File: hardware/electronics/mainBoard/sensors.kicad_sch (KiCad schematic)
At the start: 8 parts, among them J18 M8S-04PFFR-SF8001, J19 STEMMA-QT, J20 STEMMA-QT, J21 STEMMA-QT, J22 STEMMA-QT, J23 STEMMA-QT, U18 LPS28DFW

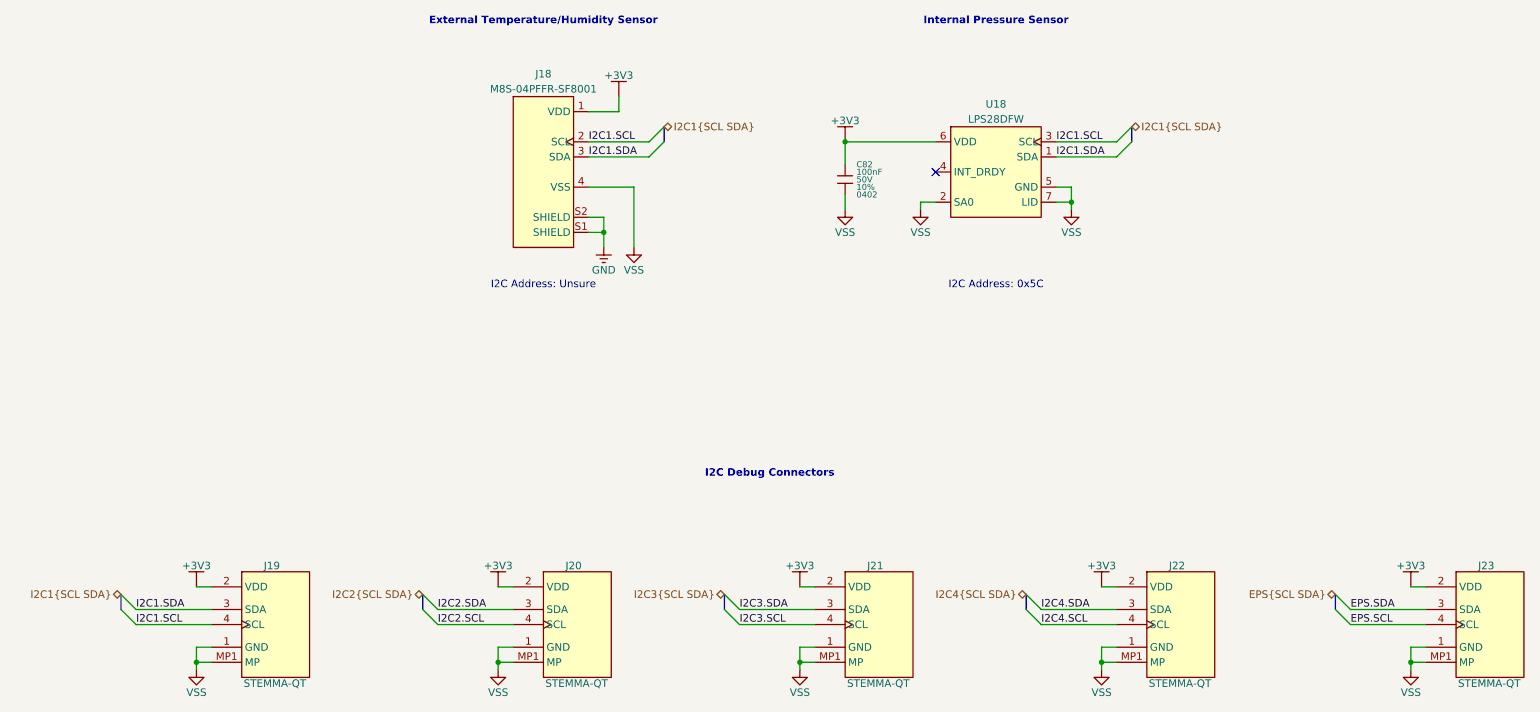
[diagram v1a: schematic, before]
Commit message: moved STEMA QT connectors to debugger sheets
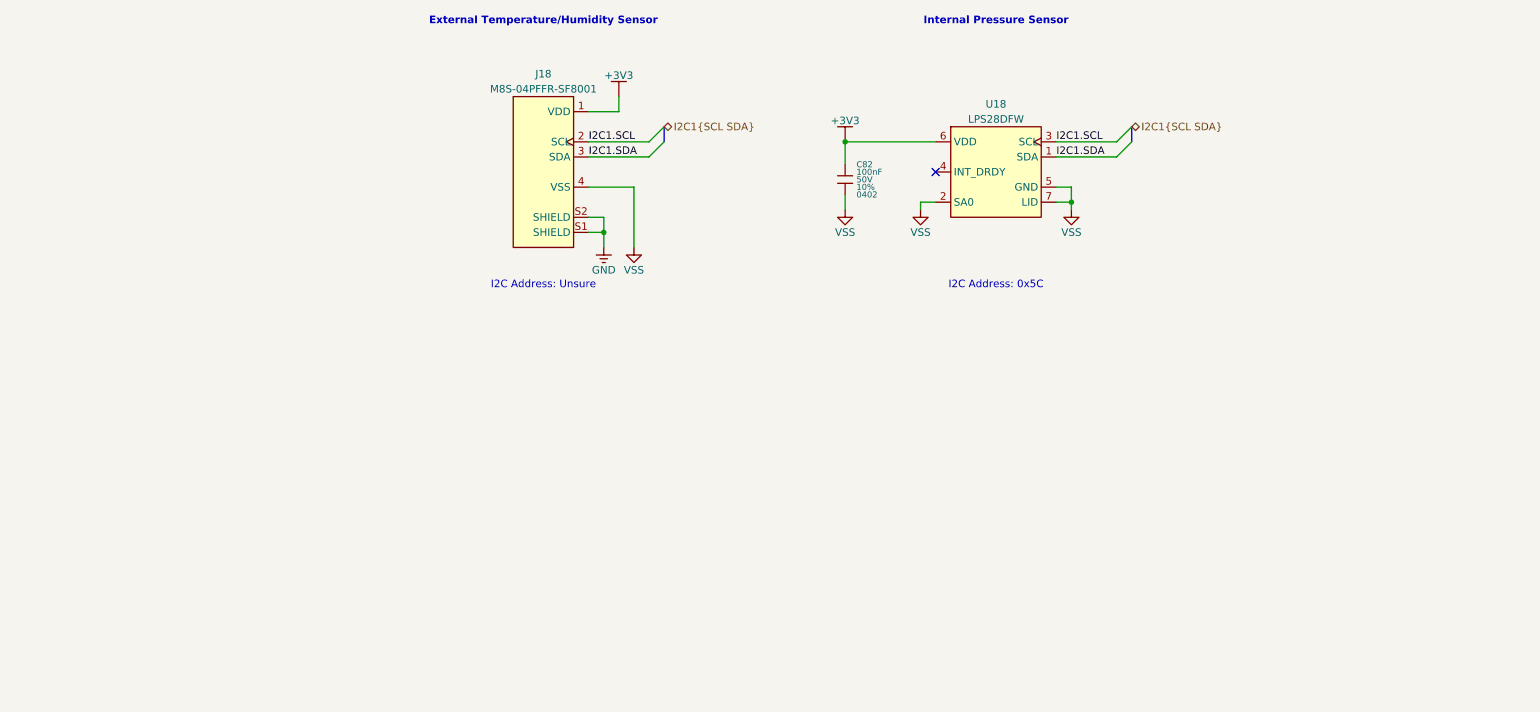
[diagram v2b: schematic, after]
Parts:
- removed J19, J20, J21, J22, J23: STEMMA-QT, lib_connectors:JST_SH_BM04B-SRSS-TB, symbol lib_sch:STEMMA-QT
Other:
- note removed: "I2C Debug Connectors"

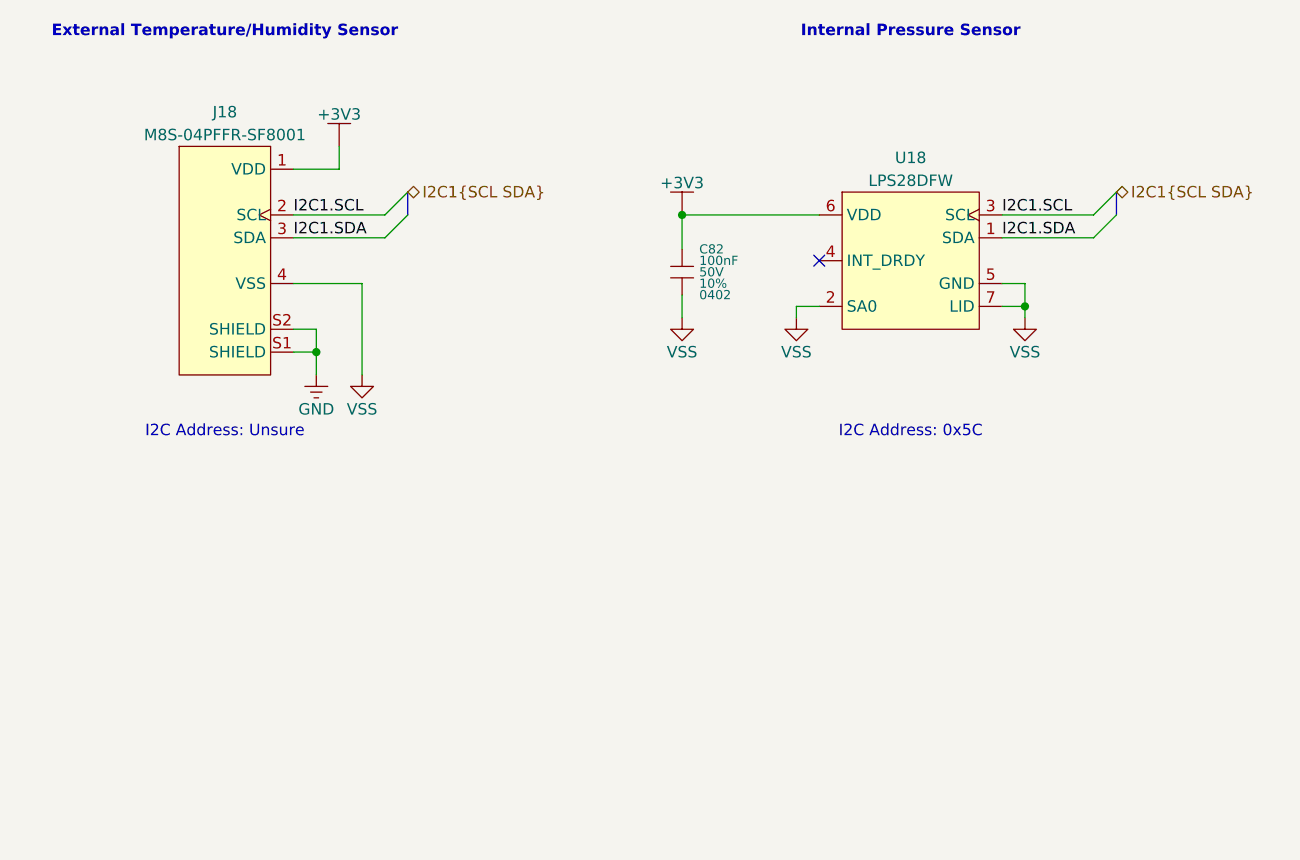
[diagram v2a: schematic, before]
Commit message: fixed net names and added notes
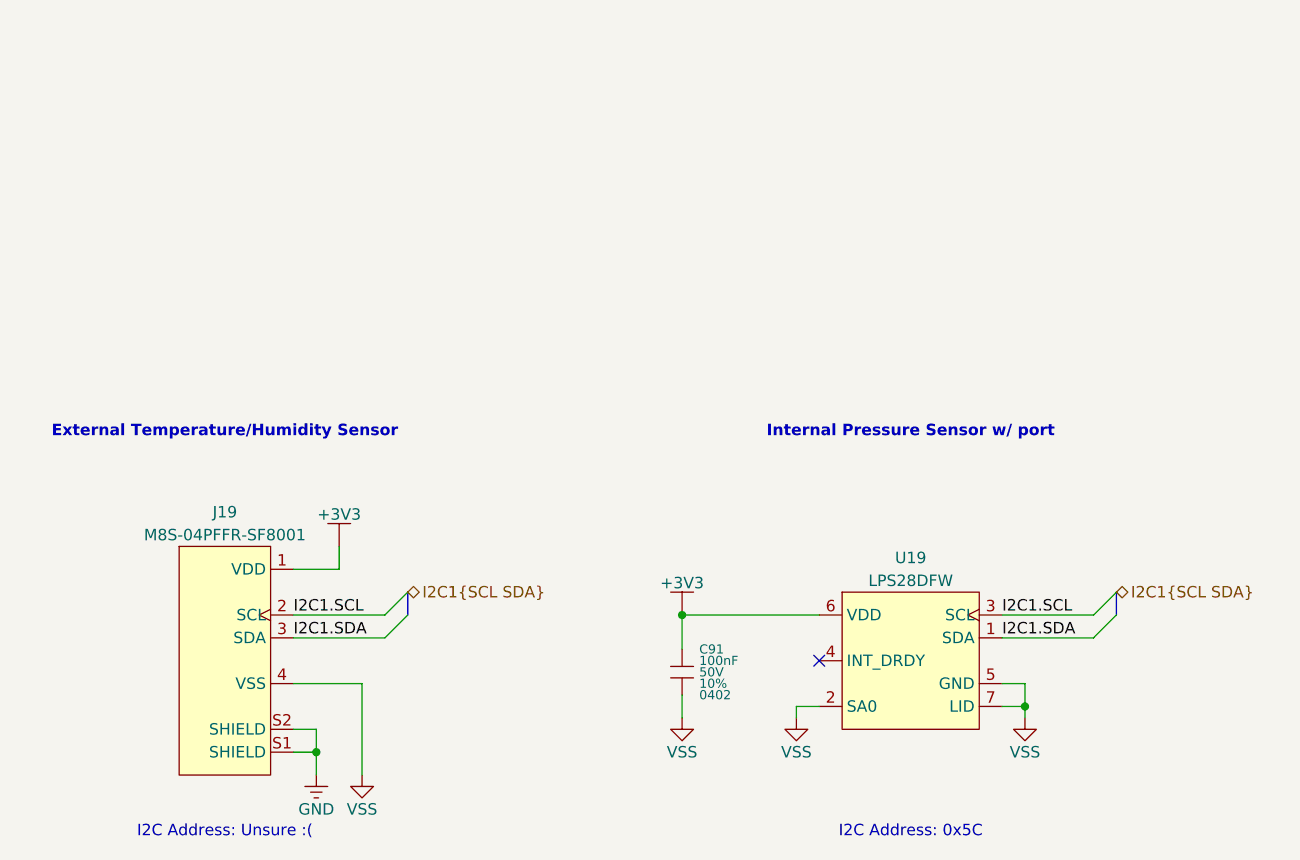
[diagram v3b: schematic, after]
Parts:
- renumbered C82 to C91, J18 to J19, U18 to U19
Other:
- note added: "I2C Address: Unsure :("
- note added: "Internal Pressure Sensor w/ port"
- note removed: "I2C Address: Unsure"
- note removed: "Internal Pressure Sensor"
- moved on the sheet: C91, J19, U19

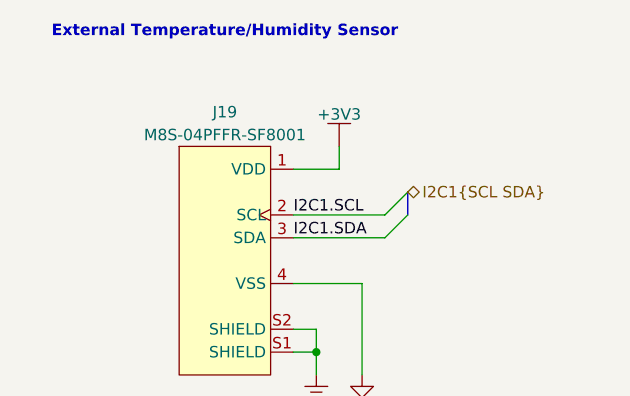
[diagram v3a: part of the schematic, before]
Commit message: renumber references
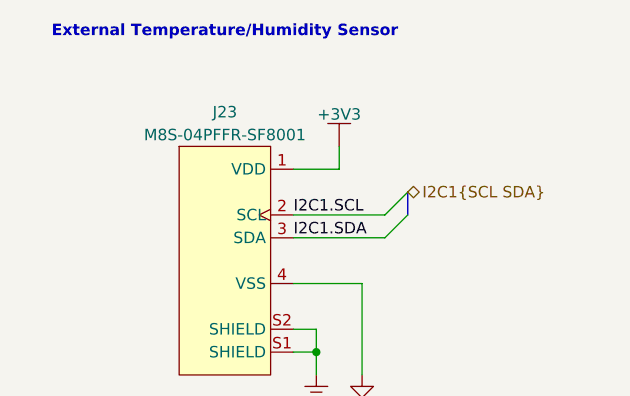
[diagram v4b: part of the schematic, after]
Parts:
- renumbered J19 to J23
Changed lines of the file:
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@@
 		(dnp no)
 		(fields_autoplaced yes)
-		(property "Reference" "#PWR0211"
+		(property "Reference" "#PWR0219"
 			(at 152.4 114.3 0)
 			(effects
@@
 			(project "mainBoard"
 				(path "/be16e32f-2ccf-4272-9ec7-94d5fe7a55e0/4fa91b0b-0224-4171-b5d2-5ca4be681229"
-					(reference "#PWR0211")
+					(reference "#PWR0219")
 					(unit 1)
 				)
@@
 		(dnp no)
 		(fields_autoplaced yes)
-		(property "Reference" "#PWR0209"
+		(property "Reference" "#PWR0217"
 			(at 114.3 95.25 0)
 			(effects
@@
 			(project "mainBoard"
 				(path "/be16e32f-2ccf-4272-9ec7-94d5fe7a55e0/4fa91b0b-0224-4171-b5d2-5ca4be681229"
-					(reference "#PWR0209")
+					(reference "#PWR0217")
 					(unit 1)
 				)
@@
 		(dnp no)
 		(fields_autoplaced yes)
-		(property "Reference" "J19"
+		(property "Reference" "J23"
 			(at 101.6 91.44 0)
 			(do_not_autoplace yes)
@@
 			(project "mainBoard"
 				(path "/be16e32f-2ccf-4272-9ec7-94d5fe7a55e0/4fa91b0b-0224-4171-b5d2-5ca4be681229"
-					(reference "J19")
+					(reference "J23")
 					(unit 1)
 				)
@@
 		(dnp no)
 		(fields_autoplaced yes)
-		(property "Reference" "#PWR0215"
+		(property "Reference" "#PWR0223"
 			(at 116.84 120.65 0)
 			(effects
@@
 			(project "mainBoard"
 				(path "/be16e32f-2ccf-4272-9ec7-94d5fe7a55e0/4fa91b0b-0224-4171-b5d2-5ca4be681229"
-					(reference "#PWR0215")
+					(reference "#PWR0223")
 					(unit 1)
 				)
@@
 		(dnp no)
 		(fields_autoplaced yes)
-		(property "Reference" "#PWR0213"
+		(property "Reference" "#PWR0221"
 			(at 190.5 114.3 0)
 			(effects
@@
 			(project "mainBoard"
 				(path "/be16e32f-2ccf-4272-9ec7-94d5fe7a55e0/4fa91b0b-0224-4171-b5d2-5ca4be681229"
-					(reference "#PWR0213")
+					(reference "#PWR0221")
 					(unit 1)
 				)
@@
 		(dnp no)
 		(fields_autoplaced yes)
-		(property "Reference" "#PWR0214"
+		(property "Reference" "#PWR0222"
 			(at 111.76 120.65 0)
 			(effects
@@
 			(project ""
 				(path "/be16e32f-2ccf-4272-9ec7-94d5fe7a55e0/4fa91b0b-0224-4171-b5d2-5ca4be681229"
-					(reference "#PWR0214")
+					(reference "#PWR0222")
 					(unit 1)
 				)
@@
 		(dnp no)
 		(fields_autoplaced yes)
-		(property "Reference" "#PWR0210"
+		(property "Reference" "#PWR0218"
 			(at 152.4 102.87 0)
 			(effects
@@
 			(project "mainBoard"
 				(path "/be16e32f-2ccf-4272-9ec7-94d5fe7a55e0/4fa91b0b-0224-4171-b5d2-5ca4be681229"
-					(reference "#PWR0210")
+					(reference "#PWR0218")
 					(unit 1)
 				)
@@
 		(dnp no)
 		(fields_autoplaced yes)
-		(property "Reference" "#PWR0212"
+		(property "Reference" "#PWR0220"
 			(at 165.1 114.3 0)
 			(effects
@@
 			(project "mainBoard"
 				(path "/be16e32f-2ccf-4272-9ec7-94d5fe7a55e0/4fa91b0b-0224-4171-b5d2-5ca4be681229"
-					(reference "#PWR0212")
-					(unit 1)
-				)
+					(reference "#PWR0220")
+					(unit 1)
+				)
